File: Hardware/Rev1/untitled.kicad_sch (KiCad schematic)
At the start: 6 parts, among them J6 Female Conn, U6 MCP2542FD-E/SN

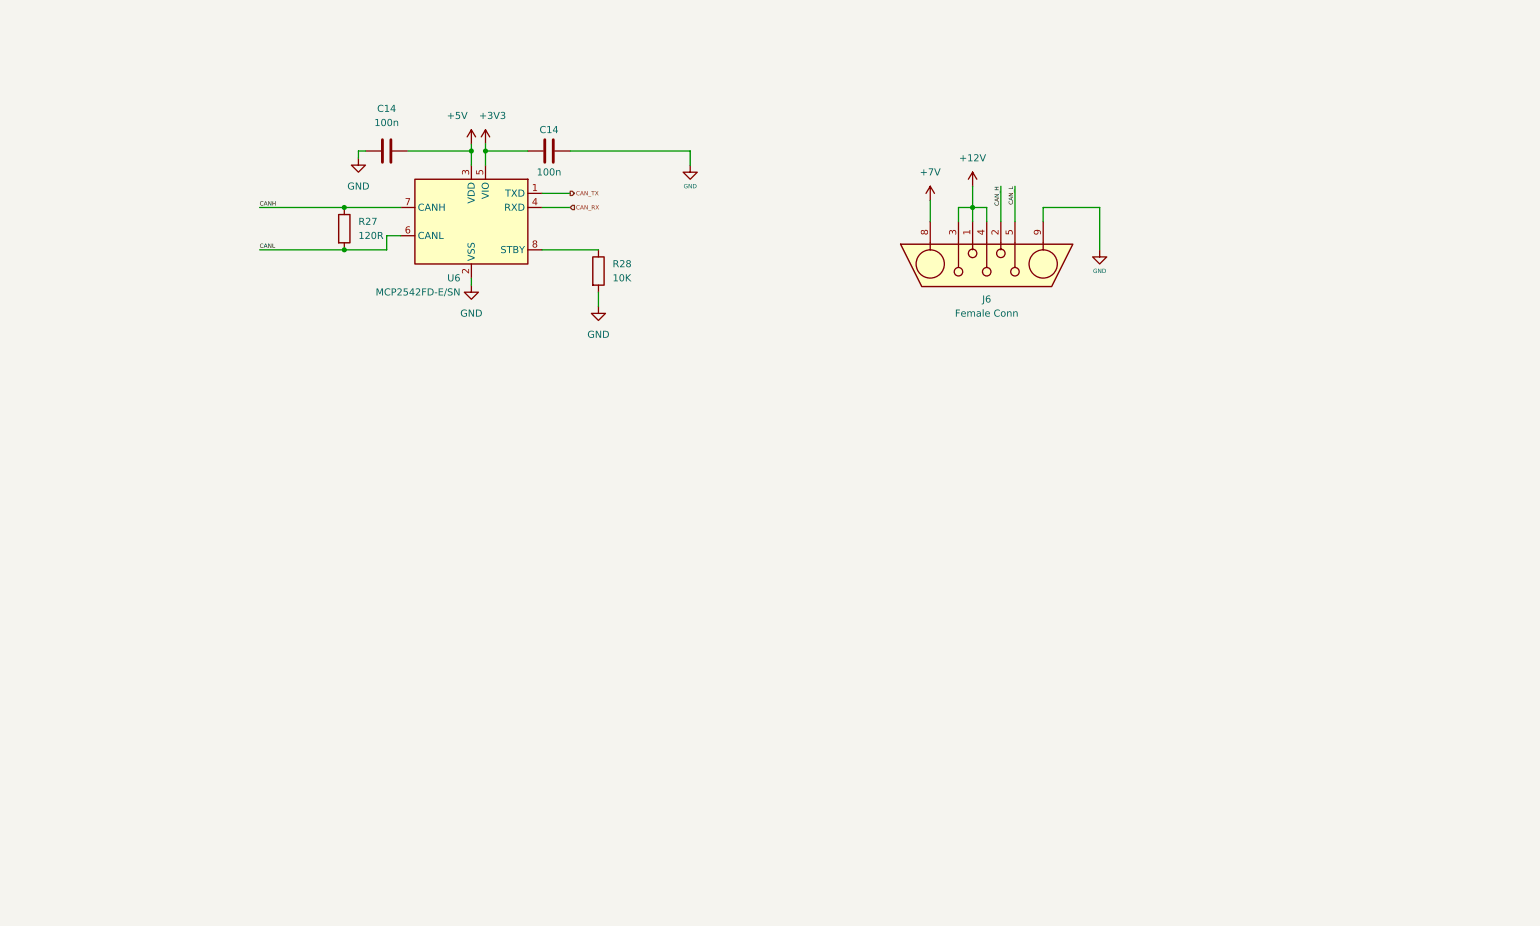
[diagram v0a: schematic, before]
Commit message: updated current limiter design and added pull-ups to OLED screen
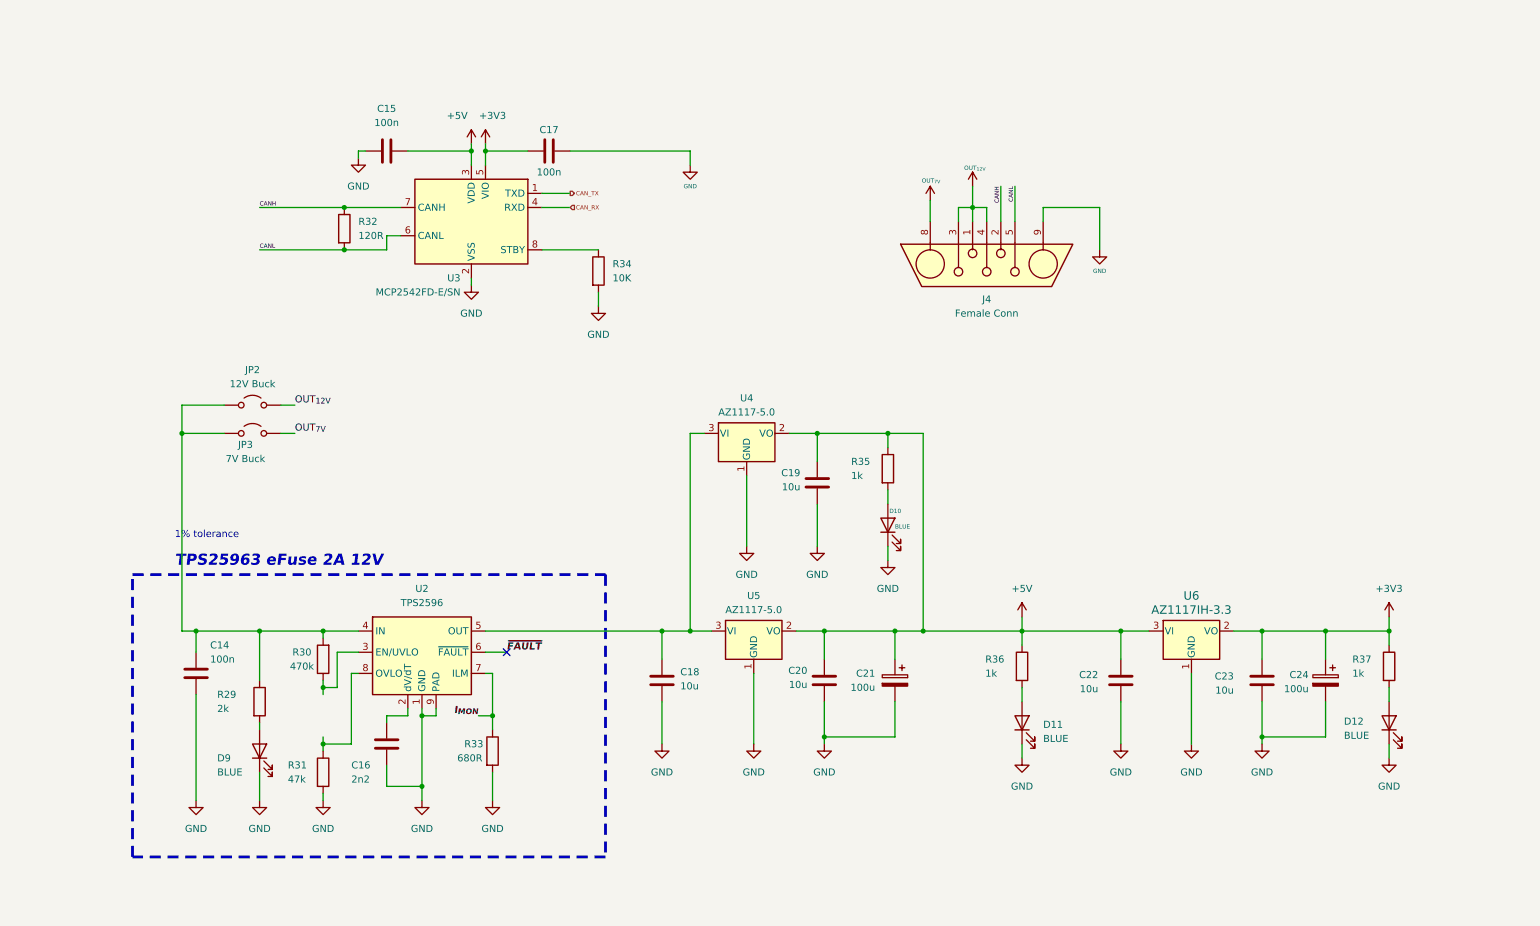
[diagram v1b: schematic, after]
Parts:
- added C14: 100n, Capacitor_SMD:C_0603_1608Metric, symbol Device:C
- added C16: 2n2, Capacitor_SMD:C_0603_1608Metric, symbol Device:C
- added C18, C19, C20, C22, C23: 10u, Capacitor_SMD:C_0805_2012Metric, symbol Device:C
- added C21, C24: 100u, Capacitor_SMD:CP_Elec_6.3x9.9, symbol Device:C_Polarized
- added D10, D11, D12, D9: BLUE, LED_SMD:LED_0603_1608Metric, symbol Device:LED
- added JP2: 12V Buck, ecocad_lib_footprints:J_0603_Triangular, symbol Jumper:Jumper_2_Open
- added JP3: 7V Buck, ecocad_lib_footprints:J_0603_Triangular, symbol Jumper:Jumper_2_Open
- added R29: 2k, Resistor_SMD:R_0603_1608Metric, symbol Device:R
- added R30: 470k, Resistor_SMD:R_0603_1608Metric, symbol Device:R
- added R31: 47k, Resistor_SMD:R_0603_1608Metric, symbol Device:R
- added R33: 680R, Resistor_SMD:R_0603_1608Metric, symbol Device:R
- added R35, R36, R37: 1k, Resistor_SMD:R_0603_1608Metric, symbol Device:R
- added U2: TPS2596, Package_SO:TI_SO-PowerPAD-8, symbol H2_Parts:TPS2596
- added U4, U5: AZ1117-5.0, Package_TO_SOT_SMD:SOT-223-3_TabPin2, symbol Regulator_Linear:AZ1117-5.0
- added U6: AZ1117IH-3.3, Package_TO_SOT_SMD:SOT-223-3_TabPin2, symbol ecocad_lib_symbols:AZ1117IH-3.3
- R34: renamed from R28; footprint (none) -> Resistor_SMD:R_0603_1608Metric
- renumbered C14 to C15, C14 to C17, J6 to J4, R27 to R32, U6 to U3
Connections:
- net CAN_H is gone; now on net CANH: J4.2
- net CAN_L is gone; now on net CANL: J4.5
- net +3V3: now also C23.1, C24.1, R37.1, U6.2 (VO)
- net +5V: now also C19.1, C20.1, C21.1, C22.1, R35.1, R36.1, U4.2 (VO), U5.2 (VO), U6.3 (VI)
- net GND: now also C14.2, C16.2, C18.2, C19.2, C20.2, C21.2, C22.2, C23.2, C24.2, D10.1 (K), D11.1 (K), D12.1 (K), D9.1 (K), R31.2, R33.2, U2.1 (GND), U2.9 (PAD), U4.1 (GND), U5.1 (GND), U6.1 (GND)
- net +12V renamed OUT_{12V}
- net OUT_{12V}: now also JP2.2 (B)
- net +7V renamed OUT_{7V}
- net OUT_{7V}: now also JP3.2 (B)
- new net: C18.1, U2.5 (OUT), U4.3 (VI), U5.3 (VI)
- new net: D12.2 (A), R37.2
- new net: C14.1, JP2.1 (A), JP3.1 (A), R29.1, R30.2, U2.4 (IN)
- new net: D10.2 (A), R35.2
- new net: R30.1, U2.3 (EN/UVLO)
- new net: C16.1, U2.2 (dV/dT)
- new net: R31.1, U2.8 (OVLO)
- new net: D11.2 (A), R36.2
- new net: D9.2 (A), R29.2
- new net I_{MON}: R33.1, U2.7 (ILM)
- new net ~{FAULT}: U2.6 (~{FAULT})
- no-connect marks 0 -> 1
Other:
- note added: "1% tolerance"
- note added: "TPS25963 eFuse 2A 12V"

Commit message: Ideal didode controller
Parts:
- renumbered C14 to C23, C15 to C24, C16 to C25, C17 to C26, C18 to C27, C19 to C28, C20 to C29, C21 to C30, C22 to C31, C23 to C32, C24 to C33, R29 to R34, R30 to R35, R31 to R36, R32 to R37, R33 to R38, R34 to R39, R35 to R40, R36 to R41, R37 to R42, U2 to U3, U3 to U4, U4 to U5, U5 to U6, U6 to U7

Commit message: Changed layout worksesh Jan 3rd 2026
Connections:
- net +12V: now reaches C27.1, U3.5 (OUT), U5.3 (VI), U6.3 (VI)
- net FUSE_IN: now reaches C23.1, JP2.1 (A), JP3.1 (A), R34.1, R35.2, U3.4 (IN)
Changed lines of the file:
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@@
 	)
 	(junction
+		(at 127 123.19)
+		(diameter 0)
+		(color 0 0 0 0)
+	)
+	(junction
 		(at 186.69 46.99)
 		(diameter 0)
@@
 	(wire
 		(pts
+			(xy 127 123.19) (xy 130.81 123.19)
+		)
+		(stroke
+			(width 0)
+			(type default)
+		)
+	)
+	(wire
+		(pts
 			(xy 87.63 151.13) (xy 87.63 153.67)
 		)
@@
 	(wire
 		(pts
+			(xy 177.8 123.19) (xy 195.58 123.19)
+		)
+		(stroke
+			(width 0)
+			(type default)
+		)
+	)
+	(wire
+		(pts
 			(xy 160.02 123.19) (xy 172.72 123.19)
 		)
@@
 	(wire
 		(pts
-			(xy 177.8 123.19) (xy 195.58 123.19)
-		)
-		(stroke
-			(width 0)
-			(type default)
-		)
-	)
-	(wire
-		(pts
 			(xy 85.09 36.83) (xy 96.52 36.83)
 		)
@@
 	(wire
 		(pts
-			(xy 44.45 87.63) (xy 44.45 123.19)
+			(xy 172.72 123.19) (xy 177.8 123.19)
 		)
 		(stroke
@@
 	(wire
 		(pts
-			(xy 44.45 123.19) (xy 46.99 123.19)
+			(xy 44.45 87.63) (xy 44.45 123.19)
 		)
 		(stroke
@@
 	(wire
 		(pts
-			(xy 44.45 82.55) (xy 52.07 82.55)
+			(xy 44.45 123.19) (xy 46.99 123.19)
 		)
 		(stroke
@@
 	(wire
 		(pts
-			(xy 171.45 90.17) (xy 171.45 87.63)
+			(xy 44.45 82.55) (xy 52.07 82.55)
 		)
 		(stroke
@@
 	(wire
 		(pts
-			(xy 184.15 49.53) (xy 184.15 46.99)
+			(xy 171.45 90.17) (xy 171.45 87.63)
 		)
 		(stroke
@@
 	(wire
 		(pts
-			(xy 58.42 54.61) (xy 73.66 54.61)
+			(xy 184.15 49.53) (xy 184.15 46.99)
 		)
 		(stroke
@@
 	(wire
 		(pts
-			(xy 69.85 143.51) (xy 74.93 143.51)
+			(xy 58.42 54.61) (xy 73.66 54.61)
 		)
 		(stroke
@@
 	(wire
 		(pts
-			(xy 172.72 123.19) (xy 177.8 123.19)
+			(xy 69.85 143.51) (xy 74.93 143.51)
 		)
 		(stroke
@@
 	(wire
 		(pts
-			(xy 99.06 123.19) (xy 130.81 123.19)
+			(xy 99.06 123.19) (xy 127 123.19)
 		)
 		(stroke
@@
 		)
 	)
+	(label "FUSE_IN"
+		(at 44.45 101.6 90)
+		(effects
+			(font
+				(size 0.762 0.762)
+			)
+			(justify left bottom)
+		)
+	)
 	(label "CANH"
 		(at 191.77 43.18 270)
@@
 		)
 	)
+	(label "5V_OUT"
+		(at 161.29 123.19 0)
+		(effects
+			(font
+				(size 0.762 0.762)
+			)
+			(justify left bottom)
+		)
+	)
 	(label "CANL"
 		(at 58.42 54.61 0)
@@
 		)
 	)
+	(label "FUSE_OUT"
+		(at 104.14 123.19 0)
+		(effects
+			(font
+				(size 0.762 0.762)
+			)
+			(justify left bottom)
+		)
+	)
 	(label "OUT_{12V}"
 		(at 64.77 82.55 0)
@@
 					(unit 1)
 				)
+			)
+		)
+	)
+	(symbol
+		(lib_id "power:+12V")
+		(at 127 123.19 0)
+		(unit 1)
+		(exclude_from_sim no)
+		(in_bom yes)
+		(on_board yes)
+		(dnp no)
+		(fields_autoplaced yes)
+		(property "Reference" "#PWR044"
+			(at 127 127 0)
+			(effects
+				(font
+					(size 1.27 1.27)
+				)
+				(hide yes)
+			)
+		)
+		(property "Value" "+12V"
+			(at 127 118.11 0)
+			(effects
+				(font
+					(size 1.27 1.27)
+				)
+			)
+		)
+		(property "Footprint" ""
+			(at 127 123.19 0)
+			(effects
+				(font
+					(size 1.27 1.27)
+				)
+				(hide yes)
+			)
+		)
+		(property "Datasheet" ""
+			(at 127 123.19 0)
+			(effects
+				(font
+					(size 1.27 1.27)
+				)
+				(hide yes)
+			)
+		)
+		(property "Description" "Power symbol creates a global label with name \"+12V\""
+			(at 127 123.19 0)
+			(effects
+				(font
+					(size 1.27 1.27)
+				)
+				(hide yes)
+			)
+		)
+		(pin "1"
+		)
+		(instances
+			(project "defogger_and_wiper"
+				(path "/41c72644-20f5-42d1-bef2-b0cf00d5a631/374727e2-a35d-4157-afab-761aee5465d8"
+					(reference "#PWR044")
+					(unit 1)
+				)

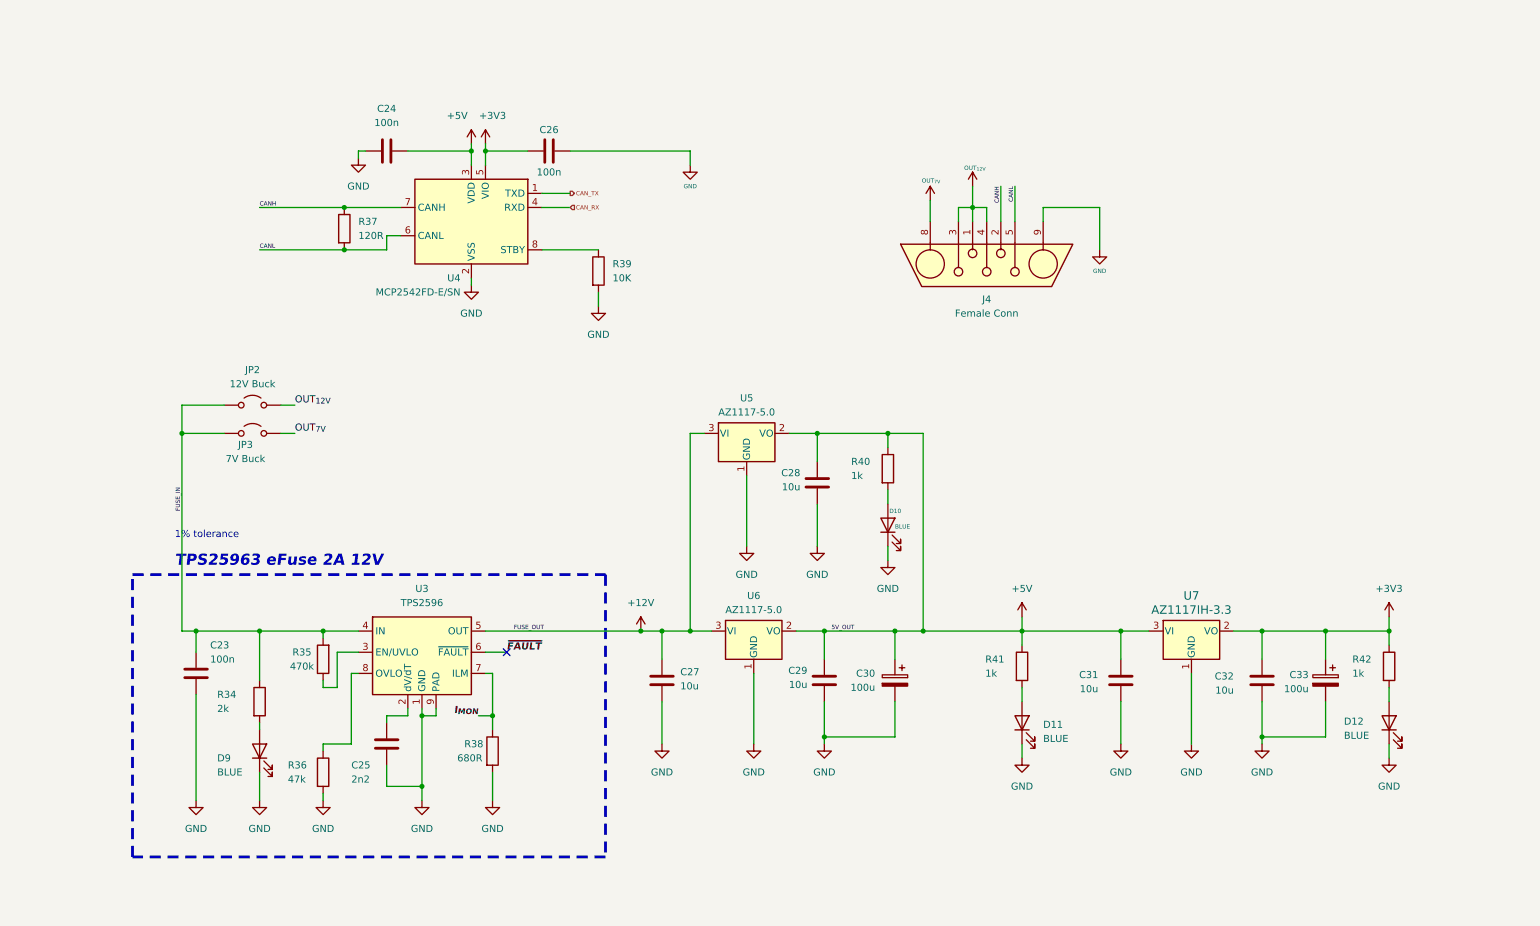
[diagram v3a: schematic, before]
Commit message: connectors changed, routing to do
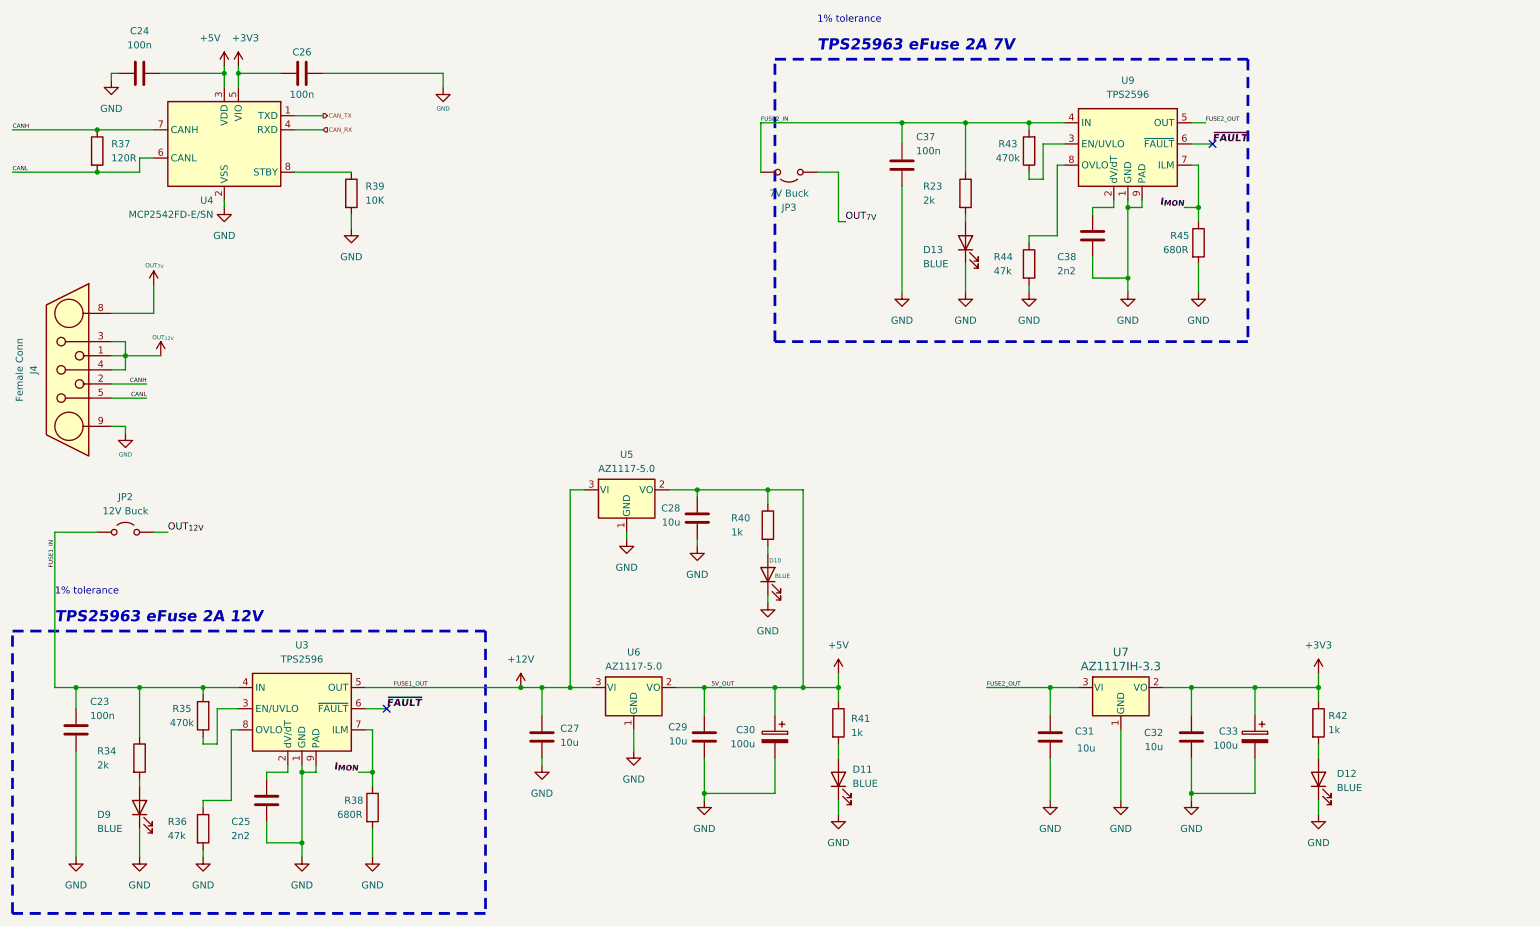
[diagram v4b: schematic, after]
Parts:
- added C37: 100n, Capacitor_SMD:C_0603_1608Metric, symbol Device:C
- added C38: 2n2, Capacitor_SMD:C_0603_1608Metric, symbol Device:C
- added D13: BLUE, LED_SMD:LED_0603_1608Metric, symbol Device:LED
- added R23: 2k, Resistor_SMD:R_0603_1608Metric, symbol Device:R
- added R43: 470k, Resistor_SMD:R_0603_1608Metric, symbol Device:R
- added R44: 47k, Resistor_SMD:R_0603_1608Metric, symbol Device:R
- added R45: 680R, Resistor_SMD:R_0603_1608Metric, symbol Device:R
- added U9: TPS2596, Package_SO:TI_SO-PowerPAD-8, symbol H2_Parts:TPS2596
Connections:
- net +5V: no longer C31.1, U7.3 (VI)
- net GND: now also C37.2, C38.2, D13.1 (K), R44.2, R45.2, U9.1 (GND), U9.9 (PAD)
- net I_{MON}: now also R45.1, U9.7 (ILM)
- net ~{FAULT}: now also U9.6 (~{FAULT})
- net FUSE_IN renamed FUSE1_IN
- net FUSE1_IN: no longer JP3.1 (A)
- new net: R44.1, U9.8 (OVLO)
- new net: C38.1, U9.2 (dV/dT)
- new net: R43.1, U9.3 (EN/UVLO)
- new net: D13.2 (A), R23.2
- new net FUSE2_IN: C37.1, JP3.1 (A), R23.1, R43.2, U9.4 (IN)
- new net FUSE2_OUT: C31.1, U7.3 (VI), U9.5 (OUT)
- no-connect marks 1 -> 2
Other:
- note added: "TPS25963 eFuse 2A 7V"
- moved on the sheet: C23, C24, C25, C26, C27, C28, C29, C30, C31, C32, C33, D10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
